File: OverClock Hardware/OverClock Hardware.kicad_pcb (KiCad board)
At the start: 4 copper layers, 100 x 100 mm, 123 parts, among them J1 USB_C_Plug, J2 JTAG_HDR, J3 Conn_01x03_Female, SW1 Switch_Momentary, SW2 Switch_Momentary, SW3 Switch_Momentary, SW4 Switch_Momentary, U1 TLV62569, U2 AP7365, U3 10M02SCE144

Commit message: Place and route Decoupling Capacitors
Placed and routed all the decoupling capacitors for the FPGA. Created Top and bottom GND planes too for better signal integrity
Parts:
- added C31: 10nF, Capacitor_SMD:C_0603_1608Metric_Pad1.05x0.95mm_HandSolder, B.Cu at (45.2, 9.93)
- added C32: 10nF, Capacitor_SMD:C_0603_1608Metric_Pad1.05x0.95mm_HandSolder, B.Cu at (42.6, 9.90)
- added C33: 10nF, Capacitor_SMD:C_0603_1608Metric_Pad1.05x0.95mm_HandSolder, B.Cu at (39.9, 9.70)
- C1, C2, C3, C4, C5, L1, Q1, Q10, Q11, Q12, Q13, Q14, Q15, Q16, Q17, Q18, Q19, Q2, Q20, Q21, Q22, Q23, Q24, Q25, Q26, Q27, Q28, Q29, Q3, Q30, Q31, Q32, Q4, Q5, Q6, Q7, Q8, Q9, R1, R10, R11, R12, R13, R14, R15, R16, R17, R18, R19, R2, R20, R21, R22, R23, R24, R25, R26, R27, R28, R29, R3, R30, R31, R32, R33, R34, R35, R36, R37, R38, R39, R4, R40, R41, R42, R5, R6, R7, R8, R9, RN1, RN2, RN3, RN4, U1, U2: moved to B.Cu
- C10, C11, C12, C13, C14, C15, C16, C17, C18, C19, C20, C21, C22, C23, C24, C25, C26, C27, C28, C29, C30, C6, C7, C8, C9: footprint Capacitor_SMD:C_0805_2012Metric_Pad1.15x1.40mm_HandSolder -> Capacitor_SMD:C_0603_1608Metric_Pad1.05x0.95mm_HandSolder
- U3: moved to F.Cu
- moved R4 322.4 mm to (22.9, 17.4), turned to 270 degrees
- moved R5 316.7 mm to (21.1, 21.2), turned to 270 degrees
- moved R6 308.3 mm to (21.1, 17.4), turned to 270 degrees
- moved R8 306.6 mm to (21.1, 52.9)
- moved R3 304.2 mm to (22.9, 21.2), turned to 90 degrees
- moved R7 300.6 mm to (21.1, 54.9)
- moved R9 300.4 mm to (29.1, 47.2), turned to 180 degrees
- moved R35 287.0 mm to (174.8, 20.0), turned to 90 degrees
- moved R37 286.4 mm to (167.8, 20.0), turned to 90 degrees
- moved R10 284.7 mm to (29.0, 51.2), turned to 180 degrees
- moved R39 274.5 mm to (164.3, 32.0), turned to 270 degrees
- moved R36 272.8 mm to (171.3, 20.0), turned to 90 degrees
- moved R38 272.2 mm to (164.3, 20.0), turned to 90 degrees
- moved R42 249.3 mm to (174.8, 32.0), turned to 270 degrees
- moved R40 244.7 mm to (167.8, 32.0), turned to 270 degrees
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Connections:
- net Net-(J2-Pad2) renamed /FPGA Interfacing/TMS
- net Net-(J2-Pad8) renamed /FPGA Interfacing/TDI
- J2 pad 4: Net-(J2-Pad4) -> /FPGA Interfacing/TCK
- J2 pad 6: Net-(J2-Pad6) -> /FPGA Interfacing/TDO
- R10 pad 1: Net-(J2-Pad4) -> +3V
- R10 pad 2: GND -> /FPGA Interfacing/H+
- R5 pad 1: +3V -> /FPGA Interfacing/TDO
- R5 pad 2: Net-(R5-Pad2) -> GND
- R6 pad 1: +3V -> /FPGA Interfacing/TCK
- R6 pad 2: Net-(R6-Pad2) -> GND
- R7 pad 2: Net-(R7-Pad2) -> /FPGA Interfacing/M-
- R8 pad 2: Net-(R8-Pad2) -> /FPGA Interfacing/M+
- R9 pad 1: Net-(J2-Pad6) -> +3V
- R9 pad 2: GND -> /FPGA Interfacing/H-
- SW1 pad 1: Net-(R5-Pad2) -> /FPGA Interfacing/M-
- SW1 pad 3: Net-(R5-Pad2) -> /FPGA Interfacing/M-
- SW2 pad 1: Net-(R6-Pad2) -> /FPGA Interfacing/M+
- SW2 pad 3: Net-(R6-Pad2) -> /FPGA Interfacing/M+
- SW3 pad 1: Net-(R7-Pad2) -> /FPGA Interfacing/H-
- SW3 pad 3: Net-(R7-Pad2) -> /FPGA Interfacing/H-
- SW4 pad 1: Net-(R8-Pad2) -> /FPGA Interfacing/H+
- SW4 pad 3: Net-(R8-Pad2) -> /FPGA Interfacing/H+
- U3 pad 10: Net-(R8-Pad2) -> Net-(U3-Pad10)
- U3 pad 111: (no net) -> +3V
- U3 pad 112: (no net) -> Net-(U3-Pad112)
- U3 pad 113: (no net) -> Net-(U3-Pad113)
- U3 pad 114: (no net) -> Net-(U3-Pad114)
- U3 pad 115: (no net) -> Net-(U3-Pad115)
- U3 pad 116: (no net) -> Net-(U3-Pad116)
- U3 pad 117: (no net) -> Net-(U3-Pad117)
- U3 pad 120: (no net) -> Net-(U3-Pad120)
- U3 pad 121: (no net) -> +3V
- U3 pad 122: (no net) -> Net-(U3-Pad122)
- U3 pad 123: (no net) -> Net-(U3-Pad123)
- U3 pad 124: (no net) -> Net-(U3-Pad124)
- U3 pad 125: (no net) -> Net-(U3-Pad125)
- U3 pad 126: (no net) -> Net-(U3-Pad126)
- U3 pad 127: (no net) -> /FPGA Interfacing/H+
- U3 pad 128: (no net) -> /FPGA Interfacing/H-
- U3 pad 129: (no net) -> /FPGA Interfacing/M+
- U3 pad 130: (no net) -> /FPGA Interfacing/M-
- U3 pad 131: (no net) -> Net-(U3-Pad131)
- U3 pad 134: (no net) -> Net-(U3-Pad134)
- U3 pad 135: (no net) -> Net-(U3-Pad135)
- U3 pad 136: (no net) -> +3V
- U3 pad 137: (no net) -> Net-(U3-Pad137)
- U3 pad 138: (no net) -> Net-(U3-Pad138)
- U3 pad 139: (no net) -> Net-(U3-Pad139)
- U3 pad 140: (no net) -> Net-(U3-Pad140)
- U3 pad 141: (no net) -> Net-(U3-Pad141)
- U3 pad 16: Net-(J2-Pad4) -> /FPGA Interfacing/TCK
- U3 pad 18: Net-(J2-Pad6) -> /FPGA Interfacing/TDO
- U3 pad 7: Net-(R5-Pad2) -> Net-(U3-Pad7)
- U3 pad 8: Net-(R6-Pad2) -> Net-(U3-Pad8)
- U3 pad 9: Net-(R7-Pad2) -> Net-(U3-Pad9)
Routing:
- net +3V: track 67.5 -> 41.7 mm, vias 3 -> 25
- net Net-(Q25-Pad3): track 0.00 -> 13.5 mm
- net Net-(Q8-Pad3): track 0.00 -> 13.4 mm
- net Net-(Q32-Pad3): track 0.00 -> 13.2 mm
- net Net-(Q24-Pad3): track 0.00 -> 13.1 mm
- net Net-(Q1-Pad3): track 0.00 -> 13.0 mm
- net Net-(Q5-Pad3): track 0.00 -> 12.9 mm
- net Net-(Q17-Pad3): track 0.00 -> 12.7 mm
- net Net-(Q29-Pad3): track 0.00 -> 12.6 mm
- net Net-(Q28-Pad3): track 0.00 -> 12.6 mm
- net Net-(Q23-Pad3): track 0.00 -> 12.6 mm
- net Net-(Q26-Pad3): track 0.00 -> 12.2 mm
- net Net-(Q20-Pad3): track 0.00 -> 11.9 mm
- net Net-(Q7-Pad3): track 0.00 -> 11.7 mm
- net Net-(Q21-Pad3): track 0.00 -> 11.7 mm
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- added copper zone on B.Cu, net +3V
- added copper zone on B.Cu, net +4V
- added copper zone on B.Cu, net GND
- added copper zone on F.Cu, net GND
- added copper zone on B.Cu, net Net-(L1-Pad1)
- removed copper zone on F.Cu, net +3V
- removed copper zone on F.Cu, net +4V
- removed copper zone on F.Cu, net Net-(L1-Pad1)
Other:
- net class Default: via_drill 0.4 -> 0.5
- net class Power: via_drill 0.4 -> 0.5

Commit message: Completed Initial Routing
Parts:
- R11, R12, R13, R14, R15, R16, R17, R18, R19, R20, R21, R22, R23, R24, R25, R26, R27, R28, R29, R3, R30, R31, R32, R33, R34, R35, R36, R37, R38, R39, R4, R40, R41, R42, R5, R6: footprint Resistor_SMD:R_0805_2012Metric_Pad1.15x1.40mm_HandSolder -> Resistor_SMD:R_0603_1608Metric_Pad1.05x0.95mm_HandSolder
- moved R42 110.4 mm to (66.5, 53.2), turned to 180 degrees
- moved R34 109.0 mm to (53.0, 53.2), turned to 180 degrees
- moved Q25 108.4 mm to (73.2, 51.2), turned to 270 degrees
- moved R41 107.8 mm to (65.0, 50.1)
- moved R26 107.5 mm to (39.9, 53.5), turned to 180 degrees
- moved Q32 107.3 mm to (67.7, 51.2), turned to 90 degrees
- moved R33 106.9 mm to (51.5, 50.5)
- moved Q24 106.4 mm to (54.1, 51.2), turned to 90 degrees
- moved Q17 106.1 mm to (59.9, 51.2), turned to 270 degrees
- moved R35 106.1 mm to (74.4, 54.1), turned to 0 degrees
- moved Q16 105.5 mm to (41.0, 51.2), turned to 90 degrees
- moved R18 105.5 mm to (26.1, 53.4), turned to 180 degrees
- moved R25 104.9 mm to (38.5, 50.5)
- moved Q9 104.8 mm to (46.4, 51.2), turned to 270 degrees
- moved R27 104.4 mm to (60.9, 54.1), turned to 0 degrees
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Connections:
- R10 pad 2: /FPGA Interfacing/H+ -> /FPGA Interfacing/M-
- R7 pad 2: /FPGA Interfacing/M- -> /FPGA Interfacing/H+
- R8 pad 2: /FPGA Interfacing/M+ -> /FPGA Interfacing/H-
- R9 pad 2: /FPGA Interfacing/H- -> /FPGA Interfacing/M+
- SW1 pad 1: /FPGA Interfacing/M- -> /FPGA Interfacing/H+
- SW1 pad 3: /FPGA Interfacing/M- -> /FPGA Interfacing/H+
- SW2 pad 1: /FPGA Interfacing/M+ -> /FPGA Interfacing/H-
- SW2 pad 3: /FPGA Interfacing/M+ -> /FPGA Interfacing/H-
- SW3 pad 1: /FPGA Interfacing/H- -> /FPGA Interfacing/M+
- SW3 pad 3: /FPGA Interfacing/H- -> /FPGA Interfacing/M+
- SW4 pad 1: /FPGA Interfacing/H+ -> /FPGA Interfacing/M-
- SW4 pad 3: /FPGA Interfacing/H+ -> /FPGA Interfacing/M-
- U3 pad 127: /FPGA Interfacing/H+ -> /FPGA Interfacing/M-
- U3 pad 128: /FPGA Interfacing/H- -> /FPGA Interfacing/M+
- U3 pad 129: /FPGA Interfacing/M+ -> /FPGA Interfacing/H-
- U3 pad 130: /FPGA Interfacing/M- -> /FPGA Interfacing/H+
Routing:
- net +4V: track 5.57 -> 171.4 mm, vias 0 -> 13
- net /FPGA Interfacing/H+: track 0.00 -> 139.6 mm, vias 0 -> 1
- net /FPGA Interfacing/H-: track 0.00 -> 139.1 mm, vias 0 -> 1
- net /FPGA Interfacing/M-: track 0.00 -> 126.8 mm, vias 0 -> 1
- net /FPGA Interfacing/M+: track 0.00 -> 126.8 mm, vias 0 -> 1
- net /FPGA Interfacing/TMS: track 0.00 -> 96.3 mm, vias 0 -> 1
- net /FPGA Interfacing/Tx: track 0.00 -> 89.6 mm, vias 0 -> 1
- net /FPGA Interfacing/TCK: track 0.00 -> 88.3 mm, vias 0 -> 1
- net /FPGA Interfacing/TDO: track 0.00 -> 85.5 mm, vias 0 -> 1
- net /FPGA Interfacing/Rx: track 0.00 -> 85.0 mm, vias 0 -> 1
- net /FPGA Interfacing/TDI: track 0.00 -> 79.7 mm, vias 0 -> 1
- net Net-(Q8-Pad1): track 1.85 -> 64.6 mm, vias 0 -> 3
- net Net-(Q7-Pad1): track 1.85 -> 64.2 mm, vias 0 -> 3
- net Net-(Q6-Pad1): track 1.85 -> 57.1 mm, vias 0 -> 3
- net Net-(Q25-Pad1): track 1.85 -> 56.2 mm, vias 0 -> 3
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- added copper zone on B.Cu, net VBUS
- removed copper zone on F.Cu, net VBUS
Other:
- board text added: "H+"
- board text added: "H-"
- board text added: "M+"
- board text added: "M-"

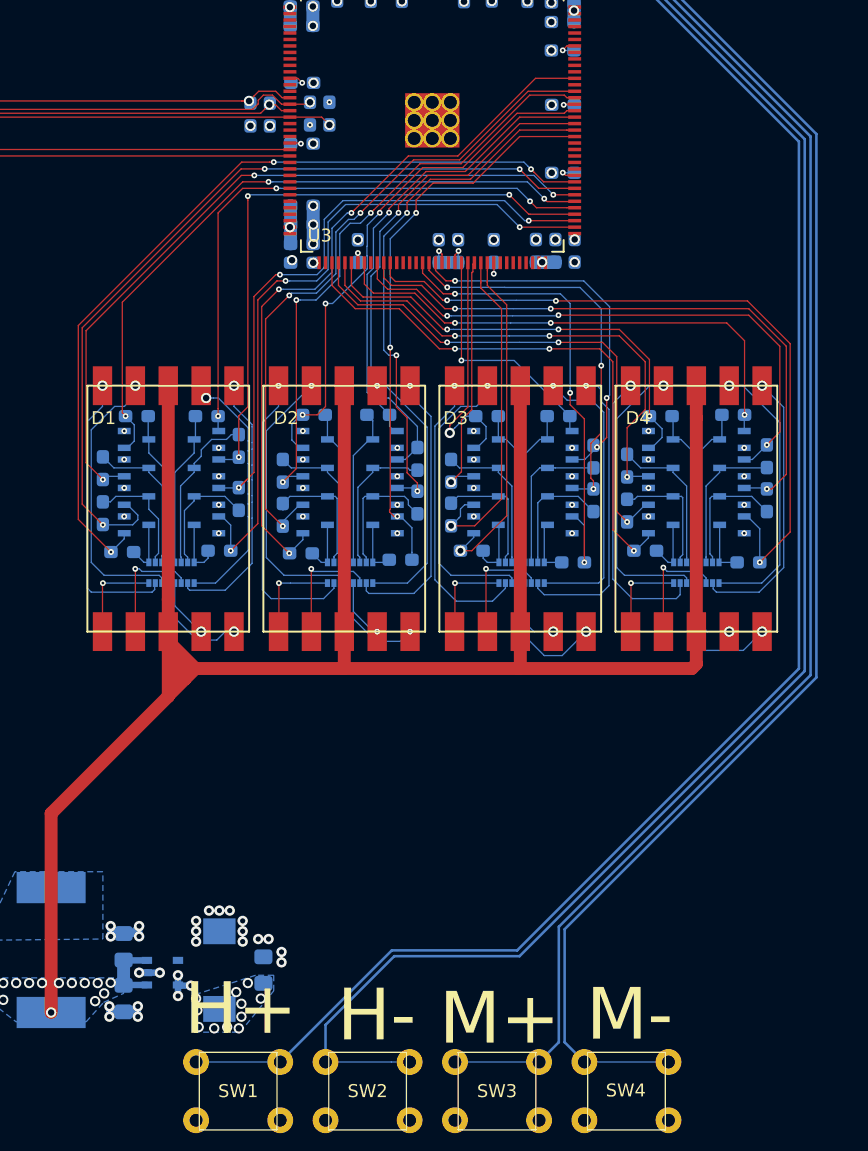
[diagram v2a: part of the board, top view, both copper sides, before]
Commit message: Rerouted 7 Segment Displays
Rearranged the displays for cleaner routing, also modified the schematic for some of the displays to allow for better routing.
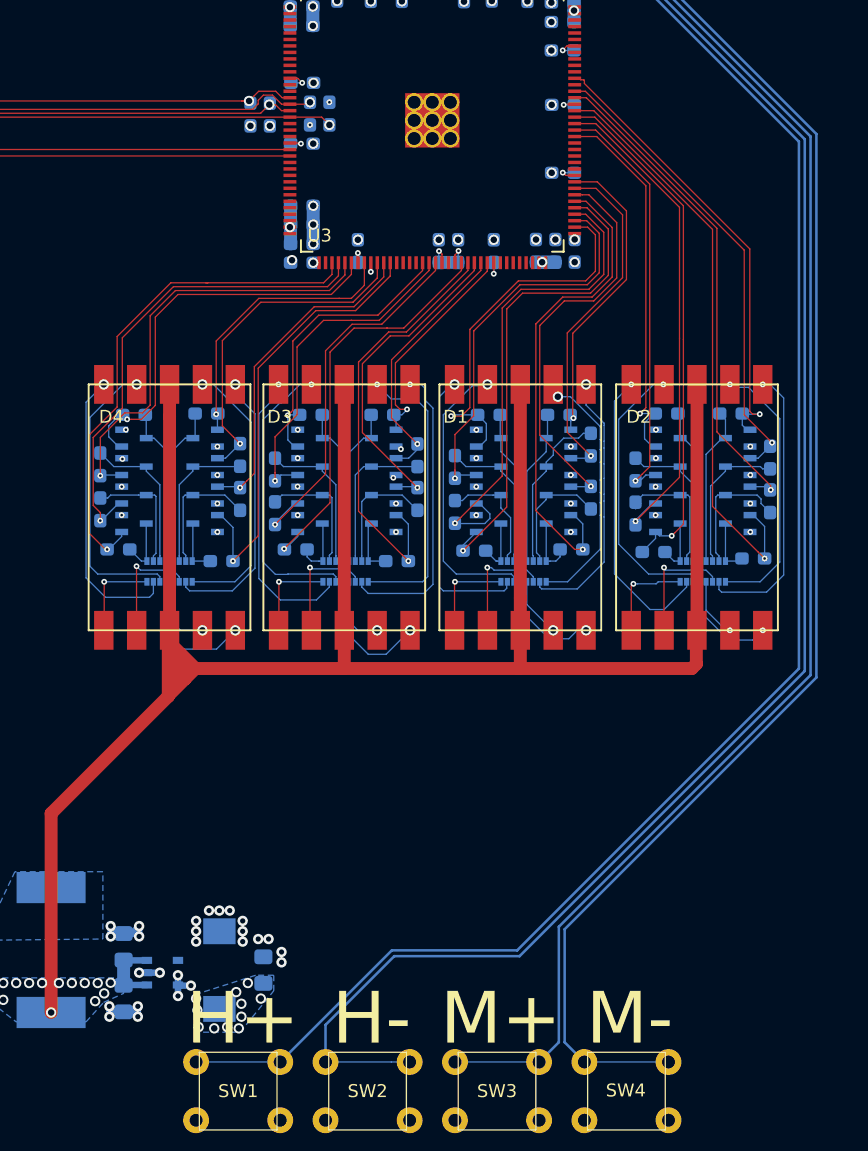
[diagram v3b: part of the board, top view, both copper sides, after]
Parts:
- moved D4 40.7 mm to (29.7, 49.9)
- moved Q25 40.7 mm to (32.5, 51.1)
- moved Q26 40.7 mm to (32.5, 49.0)
- moved Q27 40.7 mm to (32.5, 46.8)
- moved Q28 40.7 mm to (32.5, 44.5)
- moved Q29 40.7 mm to (26.9, 44.5)
- moved Q30 40.7 mm to (26.9, 46.8)
- moved Q31 40.7 mm to (26.9, 49.0)
- moved Q32 40.7 mm to (26.9, 51.1)
- moved R38 40.7 mm to (32.5, 42.6)
- moved R39 40.7 mm to (26.9, 42.8)
- moved R42 40.7 mm to (25.8, 53.1)
- moved RN4 40.7 mm to (29.7, 54.9)
- moved R35 40.7 mm to (33.7, 54.0)
- moved R36 40.7 mm to (35.1, 49.2)
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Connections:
- U3 pad 53: Net-(Q17-Pad1) -> Net-(Q21-Pad1)
- U3 pad 54: Net-(Q18-Pad1) -> Net-(Q22-Pad1)
- U3 pad 55: Net-(Q19-Pad1) -> Net-(Q23-Pad1)
- U3 pad 59: Net-(Q20-Pad1) -> Net-(Q24-Pad1)
- U3 pad 60: Net-(Q21-Pad1) -> Net-(Q17-Pad1)
- U3 pad 61: Net-(Q22-Pad1) -> Net-(Q18-Pad1)
- U3 pad 62: Net-(Q23-Pad1) -> Net-(Q19-Pad1)
- U3 pad 63: Net-(Q24-Pad1) -> Net-(Q20-Pad1)
- U3 pad 74: Net-(Q1-Pad1) -> Net-(Q5-Pad1)
- U3 pad 75: Net-(Q2-Pad1) -> Net-(Q6-Pad1)
- U3 pad 76: Net-(Q3-Pad1) -> Net-(Q7-Pad1)
- U3 pad 77: Net-(Q4-Pad1) -> Net-(Q8-Pad1)
- U3 pad 78: Net-(Q5-Pad1) -> Net-(Q1-Pad1)
- U3 pad 79: Net-(Q6-Pad1) -> Net-(Q2-Pad1)
- U3 pad 80: Net-(Q7-Pad1) -> Net-(Q3-Pad1)
- U3 pad 81: Net-(Q8-Pad1) -> Net-(Q4-Pad1)
- U3 pad 88: Net-(Q9-Pad1) -> Net-(Q13-Pad1)
- U3 pad 89: Net-(Q10-Pad1) -> Net-(Q14-Pad1)
- U3 pad 90: Net-(Q11-Pad1) -> Net-(Q15-Pad1)
- U3 pad 91: Net-(Q12-Pad1) -> Net-(Q16-Pad1)
- U3 pad 92: Net-(Q13-Pad1) -> Net-(Q9-Pad1)
- U3 pad 94: Net-(Q14-Pad1) -> Net-(Q10-Pad1)
- U3 pad 95: Net-(Q15-Pad1) -> Net-(Q11-Pad1)
- U3 pad 97: Net-(Q16-Pad1) -> Net-(Q12-Pad1)
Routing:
- net Net-(Q8-Pad1): track 64.6 -> 37.7 mm, vias 3 -> 1
- net Net-(Q7-Pad1): track 64.2 -> 37.4 mm, vias 3 -> 1
- net Net-(Q6-Pad1): track 57.1 -> 30.3 mm, vias 3 -> 1
- net Net-(Q26-Pad1): track 48.1 -> 25.4 mm, vias 3 -> 1
- net Net-(Q5-Pad1): track 51.5 -> 29.0 mm, vias 3 -> 1
- net Net-(Q25-Pad1): track 56.2 -> 33.8 mm, vias 3 -> 1
- net Net-(Q4-Pad1): track 45.8 -> 23.7 mm, vias 3 -> 1
- net Net-(Q3-Pad1): track 48.0 -> 27.1 mm, vias 3 -> 1
- net Net-(Q27-Pad1): track 44.8 -> 25.6 mm, vias 3 -> 1
- net Net-(Q28-Pad1): track 39.8 -> 21.9 mm, vias 3 -> 1
- net Net-(Q1-Pad1): track 53.8 -> 36.9 mm, vias 3 -> 1
- net Net-(Q2-Pad1): track 48.4 -> 31.5 mm, vias 3 -> 1
- net Net-(Q16-Pad1): track 55.4 -> 40.2 mm, vias 3 -> 1
- net Net-(Q14-Pad1): track 46.3 -> 32.6 mm, vias 3 -> 1
- net Net-(Q15-Pad1): track 52.0 -> 38.6 mm, vias 3 -> 1
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
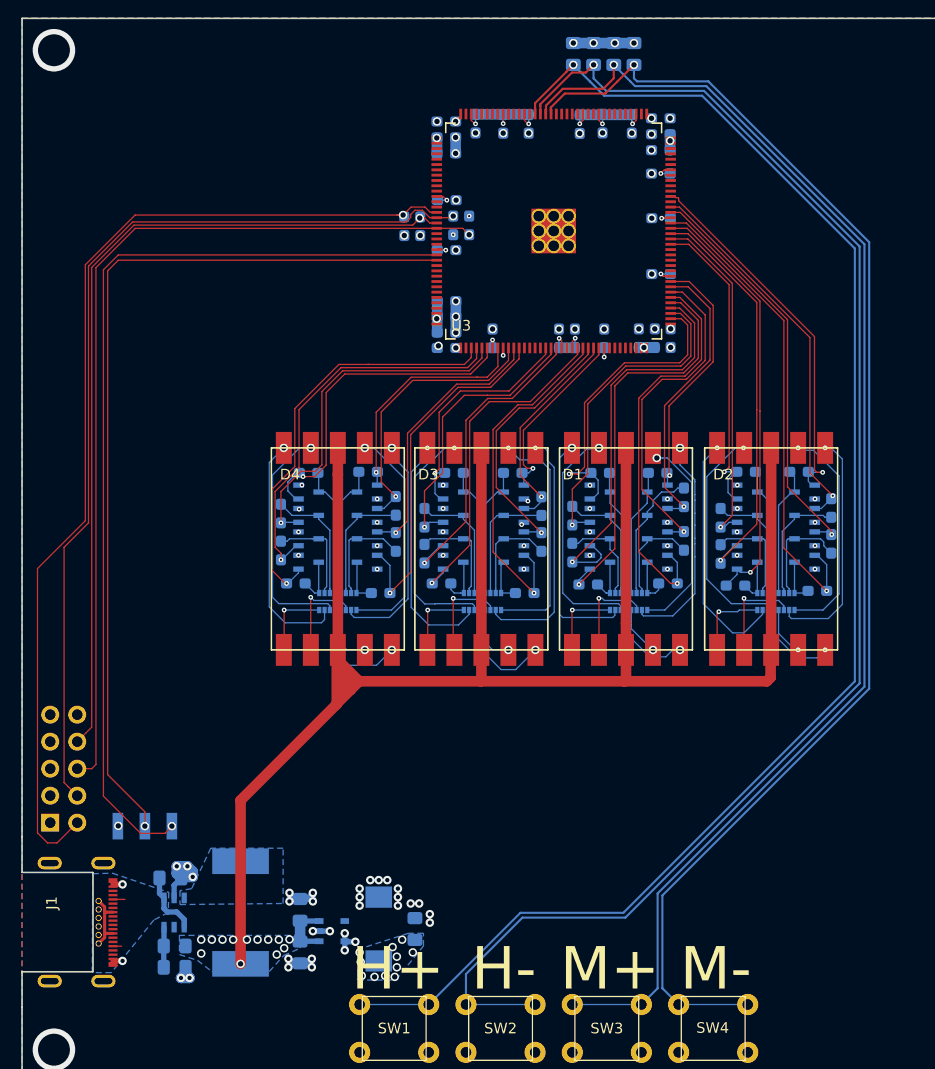
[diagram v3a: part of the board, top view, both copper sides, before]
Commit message: Added Functional Block DIagram to Schematic
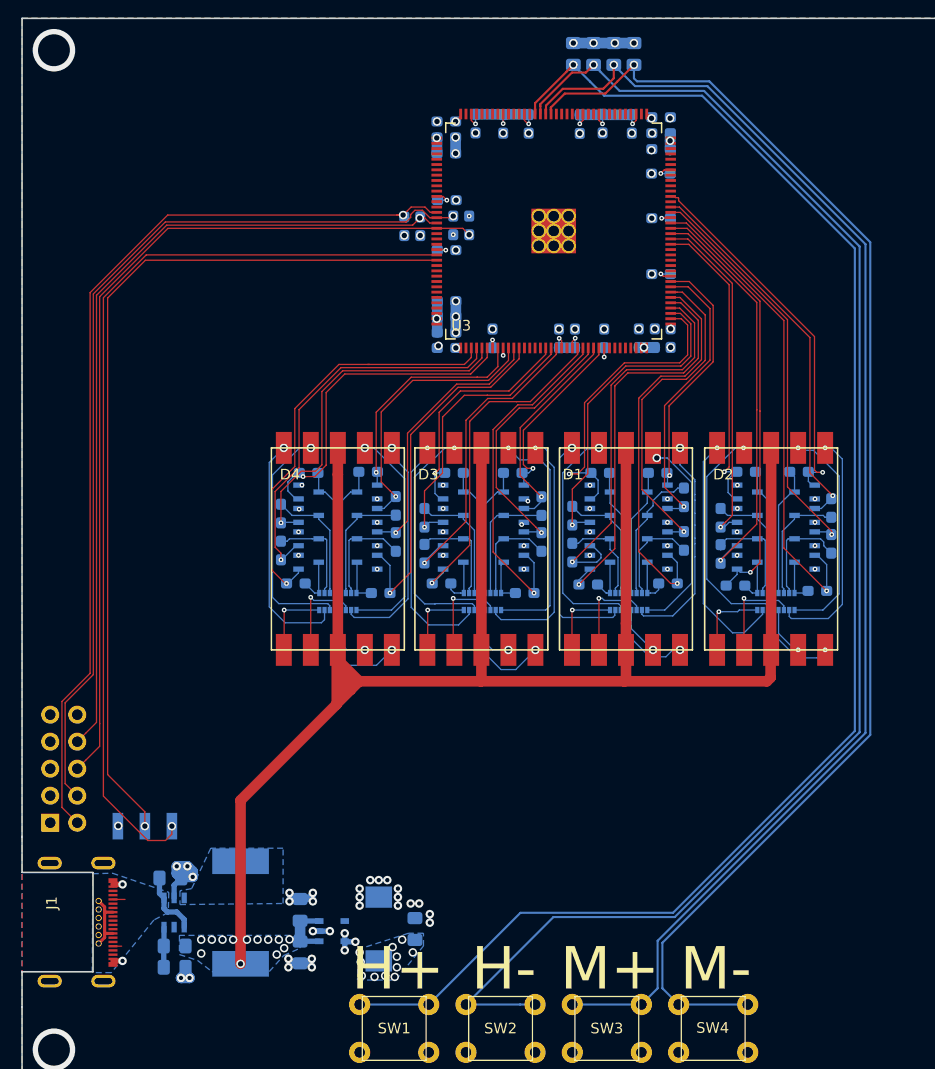
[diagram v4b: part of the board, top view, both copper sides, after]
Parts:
- moved C24 0.10 mm to (60.1, 12.3)
- moved C25 0.10 mm to (60.1, 10.8)
- moved C26 0.10 mm to (60.1, 9.30)
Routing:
- net /FPGA Interfacing/TMS: track 96.3 -> 88.3 mm
- net /FPGA Interfacing/H+: track 139.6 -> 142.4 mm
- net /FPGA Interfacing/TDO: track 85.5 -> 82.9 mm
- net /FPGA Interfacing/TCK: track 88.3 -> 86.4 mm
- net /FPGA Interfacing/TDI: track 79.7 -> 77.9 mm
- net /FPGA Interfacing/Rx: track 85.0 -> 83.5 mm
- net /FPGA Interfacing/Tx: track 89.6 -> 89.1 mm
